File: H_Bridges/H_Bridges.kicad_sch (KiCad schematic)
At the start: 28 parts, among them J1 S4B-PH-K-SLFSN, Q1 IRF540NSTRLPBF, Q2 IRF540NSTRLPBF, Q3 IRF540NSTRLPBF, Q4 IRF540NSTRLPBF, Q5 IRF540NSTRLPBF, Q6 IRF540NSTRLPBF, Q7 IRF540NSTRLPBF, Q8 IRF540NSTRLPBF, U1 ESP8266

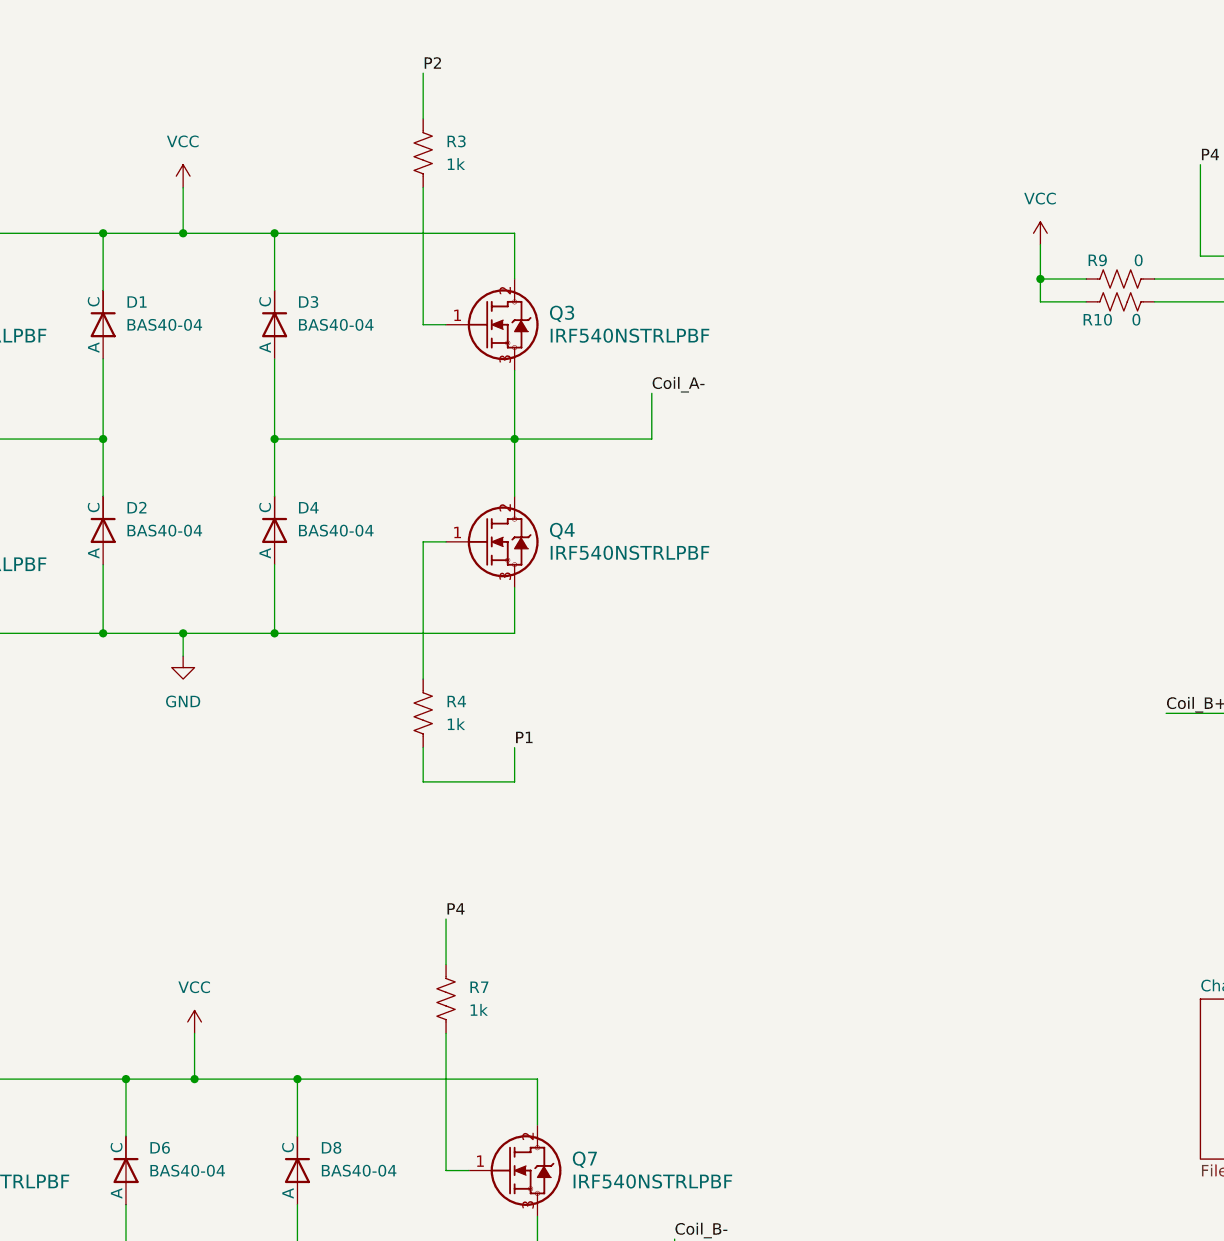
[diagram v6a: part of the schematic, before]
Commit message: designed boost converter
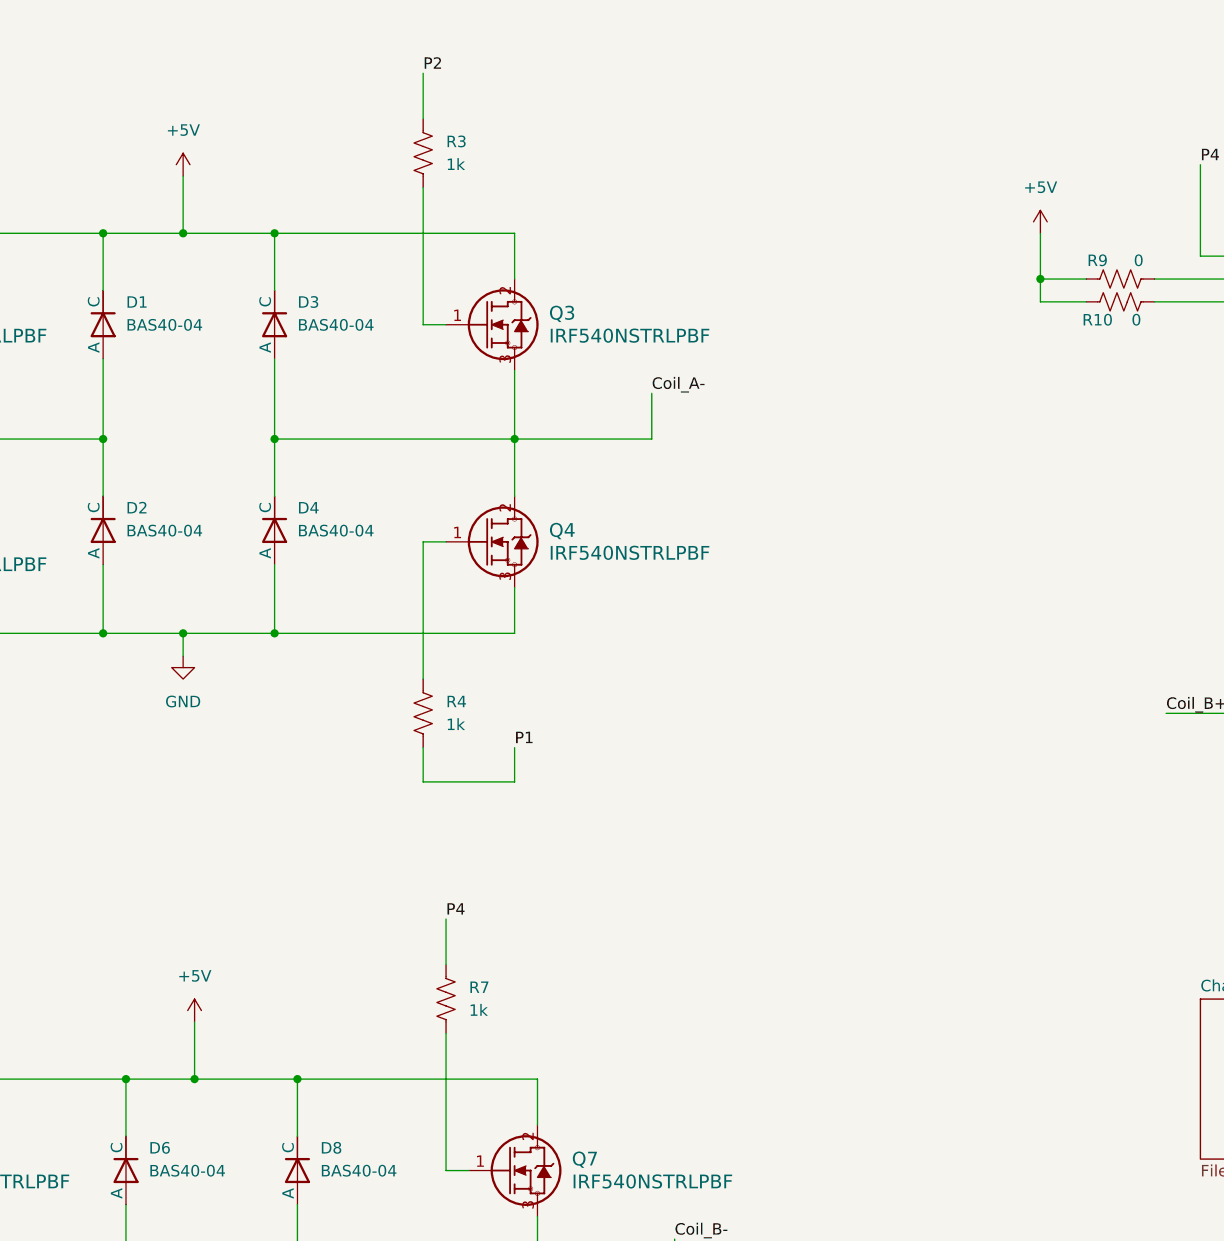
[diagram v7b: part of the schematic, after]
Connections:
- net VCC renamed +5V
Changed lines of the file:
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@@
 	(wire
 		(pts
-			(xy 87.63 35.56) (xy 87.63 40.64)
+			(xy 87.63 34.29) (xy 87.63 40.64)
 		)
 		(stroke
@@
 	(wire
 		(pts
-			(xy 182.88 41.91) (xy 182.88 45.72)
+			(xy 182.88 40.64) (xy 182.88 45.72)
+		)
+		(stroke
+			(width 0)
+			(type default)
+		)
+	)
+	(wire
+		(pts
+			(xy 88.9 128.27) (xy 88.9 134.62)
 		)
 		(stroke
@@
 		(pts
 			(xy 124.46 80.01) (xy 124.46 85.09)
-		)
-		(stroke
-			(width 0)
-			(type default)
-		)
-	)
-	(wire
-		(pts
-			(xy 88.9 129.54) (xy 88.9 134.62)
 		)
 		(stroke
@@
 				(path "/a020a591-cea5-4f16-9764-82374c05e734"
 					(reference "Q5")
-					(unit 1)
-				)
-			)
-		)
-	)
-	(symbol
-		(lib_id "power:VCC")
-		(at 182.88 41.91 0)
-		(unit 1)
-		(exclude_from_sim no)
-		(in_bom yes)
-		(on_board yes)
-		(dnp no)
-		(fields_autoplaced yes)
-		(property "Reference" "#PWR05"
-			(at 182.88 45.72 0)
-			(effects
-				(font
-					(size 1.27 1.27)
-				)
-				(hide yes)
-			)
-		)
-		(property "Value" "VCC"
-			(at 182.88 36.83 0)
-			(effects
-				(font
-					(size 1.27 1.27)
-				)
-			)
-		)
-		(property "Footprint" ""
-			(at 182.88 41.91 0)
-			(effects
-				(font
-					(size 1.27 1.27)
-				)
-				(hide yes)
-			)
-		)
-		(property "Datasheet" ""
-			(at 182.88 41.91 0)
-			(effects
-				(font
-					(size 1.27 1.27)
-				)
-				(hide yes)
-			)
-		)
-		(property "Description" "Power symbol creates a global label with name \"VCC\""
-			(at 182.88 41.91 0)
-			(effects
-				(font
-					(size 1.27 1.27)
-				)
-				(hide yes)
-			)
-		)
-		(pin "1"
-		)
-		(instances
-			(project "H_Bridges"
-				(path "/a020a591-cea5-4f16-9764-82374c05e734"
-					(reference "#PWR05")
 					(unit 1)
 				)
@@
 	)
 	(symbol
+		(lib_id "power:+5V")
+		(at 182.88 40.64 0)
+		(unit 1)
+		(exclude_from_sim no)
+		(in_bom yes)
+		(on_board yes)
+		(dnp no)
+		(fields_autoplaced yes)
+		(property "Reference" "#PWR05"
+			(at 182.88 44.45 0)
+			(effects
+				(font
+					(size 1.27 1.27)
+				)
+				(hide yes)
+			)
+		)
+		(property "Value" "+5V"
+			(at 182.88 35.56 0)
+			(effects
+				(font
+					(size 1.27 1.27)
+				)
+			)
+		)
+		(property "Footprint" ""
+			(at 182.88 40.64 0)
+			(effects
+				(font
+					(size 1.27 1.27)
+				)
+				(hide yes)
+			)
+		)
+		(property "Datasheet" ""
+			(at 182.88 40.64 0)
+			(effects
+				(font
+					(size 1.27 1.27)
+				)
+				(hide yes)
+			)
+		)
+		(property "Description" "Power symbol creates a global label with name \"+5V\""
+			(at 182.88 40.64 0)
+			(effects
+				(font
+					(size 1.27 1.27)
+				)
+				(hide yes)
+			)
+		)
+		(pin "1"
+		)
+		(instances
+			(project "H_Bridges"
+				(path "/a020a591-cea5-4f16-9764-82374c05e734"
+					(reference "#PWR05")
+					(unit 1)
+				)
+			)
+		)
+	)
+	(symbol
+		(lib_id "power:+5V")
+		(at 88.9 128.27 0)
+		(unit 1)
+		(exclude_from_sim no)
+		(in_bom yes)
+		(on_board yes)
+		(dnp no)
+		(fields_autoplaced yes)
+		(property "Reference" "#PWR010"
+			(at 88.9 132.08 0)
+			(effects
+				(font
+					(size 1.27 1.27)
+				)
+				(hide yes)
+			)
+		)
+		(property "Value" "+5V"
+			(at 88.9 123.19 0)
+			(effects
+				(font
+					(size 1.27 1.27)
+				)
+			)
+		)
+		(property "Footprint" ""
+			(at 88.9 128.27 0)
+			(effects
+				(font
+					(size 1.27 1.27)
+				)
+				(hide yes)
+			)
+		)
+		(property "Datasheet" ""
+			(at 88.9 128.27 0)
+			(effects
+				(font
+					(size 1.27 1.27)
+				)
+				(hide yes)
+			)
+		)
+		(property "Description" "Power symbol creates a global label with name \"+5V\""
+			(at 88.9 128.27 0)
+			(effects
+				(font
+					(size 1.27 1.27)
+				)
+				(hide yes)
+			)
+		)
+		(pin "1"
+		)
+		(instances
+			(project "H_Bridges"
+				(path "/a020a591-cea5-4f16-9764-82374c05e734"
+					(reference "#PWR010")
+					(unit 1)
+				)
+			)
+		)
+	)
+	(symbol
 		(lib_id "diode-nc_pin:Diode-NC_pin")
 		(at 100.33 49.53 90)
@@
 	)
 	(symbol
-		(lib_id "power:VCC")
-		(at 88.9 129.54 0)
-		(unit 1)
-		(exclude_from_sim no)
-		(in_bom yes)
-		(on_board yes)
-		(dnp no)
-		(fields_autoplaced yes)
-		(property "Reference" "#PWR010"
-			(at 88.9 133.35 0)
-			(effects
-				(font
-					(size 1.27 1.27)
-				)
-				(hide yes)
-			)
-		)
-		(property "Value" "VCC"
-			(at 88.9 124.46 0)
-			(effects
-				(font
-					(size 1.27 1.27)
-				)
-			)
-		)
-		(property "Footprint" ""
-			(at 88.9 129.54 0)
-			(effects
-				(font
-					(size 1.27 1.27)
-				)
-				(hide yes)
-			)
-		)
-		(property "Datasheet" ""
-			(at 88.9 129.54 0)
-			(effects
-				(font
-					(size 1.27 1.27)
-				)
-				(hide yes)
-			)
-		)
-		(property "Description" "Power symbol creates a global label with name \"VCC\""
-			(at 88.9 129.54 0)
-			(effects
-				(font
-					(size 1.27 1.27)
-				)
-				(hide yes)
-			)
-		)
-		(pin "1"
-		)
-		(instances
-			(project "H_Bridges"
-				(path "/a020a591-cea5-4f16-9764-82374c05e734"
-					(reference "#PWR010")
-					(unit 1)
-				)
-			)
-		)
-	)
-	(symbol
 		(lib_id "Device:R_US")
 		(at 116.84 125.73 180)
@@
 	)
 	(symbol
-		(lib_id "power:VCC")
-		(at 87.63 35.56 0)
-		(unit 1)
-		(exclude_from_sim no)
-		(in_bom yes)
-		(on_board yes)
-		(dnp no)
-		(fields_autoplaced yes)
-		(property "Reference" "#PWR09"
-			(at 87.63 39.37 0)
-			(effects
-				(font
-					(size 1.27 1.27)
-				)
-				(hide yes)
-			)
-		)
-		(property "Value" "VCC"
-			(at 87.63 30.48 0)
-			(effects
-				(font
-					(size 1.27 1.27)
-				)
-			)
-		)
-		(property "Footprint" ""
-			(at 87.63 35.56 0)
-			(effects
-				(font
-					(size 1.27 1.27)
-				)
-				(hide yes)
-			)
-		)
-		(property "Datasheet" ""
-			(at 87.63 35.56 0)
-			(effects
-				(font
-					(size 1.27 1.27)
-				)
-				(hide yes)
-			)
-		)
-		(property "Description" "Power symbol creates a global label with name \"VCC\""
-			(at 87.63 35.56 0)
-			(effects
-				(font
-					(size 1.27 1.27)
-				)
-				(hide yes)
-			)
-		)
-		(pin "1"
-		)
-		(instances
-			(project "H_Bridges"
-				(path "/a020a591-cea5-4f16-9764-82374c05e734"
-					(reference "#PWR09")
-					(unit 1)
-				)
-			)
-		)
-	)
-	(symbol
 		(lib_id "Device:R_US")
 		(at 33.02 144.78 90)
@@
 					(unit 1)
 				)
+			)
+		)
+	)
+	(symbol
+		(lib_id "power:+5V")
+		(at 87.63 34.29 0)
+		(unit 1)
+		(exclude_from_sim no)
+		(in_bom yes)
+		(on_board yes)
+		(dnp no)
+		(fields_autoplaced yes)
+		(property "Reference" "#PWR09"
+			(at 87.63 38.1 0)
+			(effects
+				(font
+					(size 1.27 1.27)
+				)
+				(hide yes)
+			)
+		)
+		(property "Value" "+5V"
+			(at 87.63 29.21 0)
+			(effects
+				(font
+					(size 1.27 1.27)
+				)
+			)
+		)
+		(property "Footprint" ""
+			(at 87.63 34.29 0)
+			(effects
+				(font
+					(size 1.27 1.27)
+				)
+				(hide yes)
+			)
+		)
+		(property "Datasheet" ""
+			(at 87.63 34.29 0)
+			(effects
+				(font
+					(size 1.27 1.27)
+				)
+				(hide yes)
+			)
+		)
+		(property "Description" "Power symbol creates a global label with name \"+5V\""
+			(at 87.63 34.29 0)
+			(effects
+				(font
+					(size 1.27 1.27)
+				)
+				(hide yes)
+			)
+		)
+		(pin "1"
+		)
+		(instances
+			(project "H_Bridges"
+				(path "/a020a591-cea5-4f16-9764-82374c05e734"
+					(reference "#PWR09")
+					(unit 1)
+				)
